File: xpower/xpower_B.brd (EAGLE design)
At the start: 80 x 80 mm, 41 parts, among them U1 TLV70233, U2 TLV70225, U3 STM1061N29, U4 ADM1085, U5 LM3674-ADJ

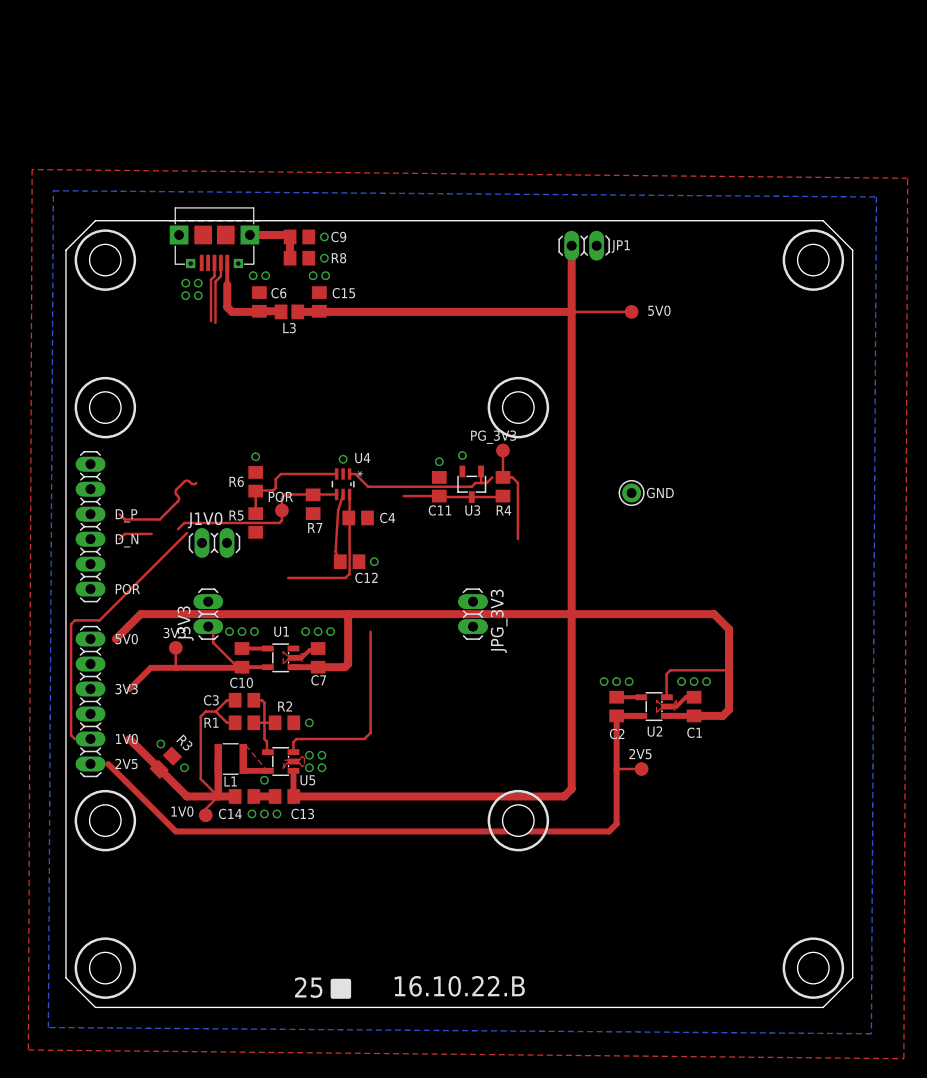
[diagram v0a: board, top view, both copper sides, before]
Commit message: xpower: B variant PCB finished
Signed-off-by: malo <pavol.malosek@gmail.com>
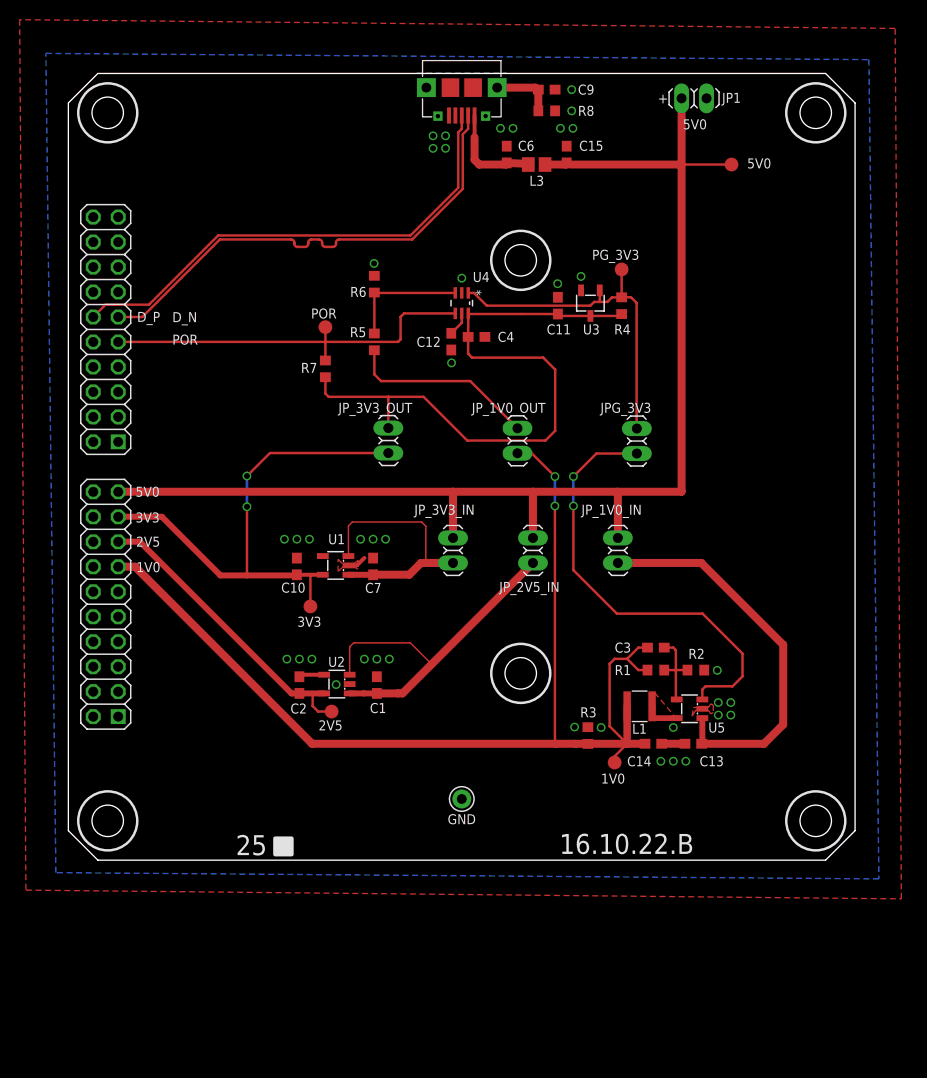
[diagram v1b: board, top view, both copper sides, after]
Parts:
- removed J1V0, J3V3: (no value), 25pinhead:1X02
- removed PWR1: (no value), 25cmsquare:LIWE_12_PIN_8X8_COMPAT
- added JP_1V0_IN, JP_2V5_IN, JP_3V3_IN: (no value), pinhead:1X02
- added JP_1V0_OUT, JP_3V3_OUT: (no value), 25pinhead:1X02
- added U$1: LIWE_40_PIN, 25cmsquare:LIWE_40_PIN_8X8
- C1, C7: value 1u, 0805 -> 1u, 0603; device rcl:C0805 -> rcl:C0603
- C10, C2: value 2u2, 0805 -> 2u2, 0603; device rcl:C0805 -> rcl:C0603
- C11, C15, C4, C6: value 100n, 0805 -> 100n, 0603; device rcl:C0805 -> rcl:C0603
- C12: value 2n2, 0805 -> 2n2, 0603; device rcl:C0805 -> rcl:C0603
- C13: value 4.7u, 0805 -> 4.7u, 0603; device rcl:C0805 -> rcl:C0603
- C14: value 10u, 0805 -> 10u, 0603; device rcl:C0805 -> rcl:C0603
- C3: value 18p, 0805 -> 18p, 0603; device rcl:C0805 -> rcl:C0603
- C9: value 4.7n, 0805 -> 4.7n, 0603; device rcl:C0805 -> rcl:C0603
- R1, R2: value 200k, 0805 -> 200k, 0603; device rcl:R0805 -> rcl:R0603
- R3: value 330, 0805 -> 330, 0603; device rcl:R0805 -> rcl:R0603
- R4, R6, R7: value 10k, 0805 -> 10k, 0603; device rcl:R0805 -> rcl:R0603
- R5: value 3k9, 0805 -> 3k9, 0603; device rcl:R0805 -> rcl:R0603
- R8: value 1M, 0805 -> 1M, 0603; device rcl:R0805 -> rcl:R0603
- moved R3 43.0 mm to (52.8, 12.7), turned to 270 degrees
- moved C3 42.2 mm to (59.7, 21.6)
- moved R1 42.2 mm to (59.7, 19.3)
- moved R2 42.2 mm to (63.8, 19.3)
- moved C13 41.9 mm to (63.6, 11.8)
- moved C14 41.9 mm to (59.5, 11.8)
- moved U5 41.9 mm to (63.2, 15.4)
- moved 1V0 41.9 mm to (55.5, 9.93)
- moved L1 41.9 mm to (59.7, 17.2)
- moved GND 35.6 mm to (40.0, 6.22)
- moved U2 32.3 mm to (27.3, 17.9)
- moved C1 32.3 mm to (31.4, 17.8)
- moved C2 32.3 mm to (23.5, 17.8)
- moved 2V5 32.1 mm to (26.8, 15.1)
- moved C15 29.3 mm to (50.7, 71.8)
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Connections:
- new net N$1: C1.1, JP_2V5_IN.1, U2.1, U2.3
- new net N$2: C7.1, JP_3V3_IN.1, U1.1, U1.3
- new net N$3: C13.1, JP_1V0_IN.1, U5.1
- net +1V0: now also JP_1V0_OUT.1, U$1.13; no longer J1V0.1, PWR1.2
- net +2V5: now also U$1.15; no longer PWR1.1
- net +3V3: now also JP_3V3_OUT.1, U$1.17; no longer J3V3.1, PWR1.4
- net +5V: now also JP_1V0_IN.2, JP_2V5_IN.2, JP_3V3_IN.2, U$1.19; no longer C1.1, C13.1, C7.1, PWR1.6, U1.1, U1.3, U2.1, U2.3, U5.1
- net D_N: now also U$1.111; no longer PWR1.9
- net D_P: now also U$1.112; no longer PWR1.10
- net GND: now also U$1.14, U$1.16, U$1.18, U$1.20; no longer PWR1.3, PWR1.8
- net J1V0: now also JP_1V0_OUT.2; no longer J1V0.2
- net J3V3: now also JP_3V3_OUT.2; no longer J3V3.2
- net POR: now also U$1.109; no longer PWR1.7
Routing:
- net +5V: track 219.1 -> 130.6 mm
- net +1V0: track 62.6 -> 116.6 mm, vias 0 -> 2
- net J3V3: track 24.7 -> 66.3 mm
- net N$3: track 0.00 -> 40.1 mm
- net D_N: track 9.81 -> 49.7 mm
- net +2V5: track 70.9 -> 31.9 mm
- net +3V3: track 22.1 -> 59.8 mm, vias 0 -> 2
- net N$1: track 0.00 -> 36.9 mm
- net D_P: track 16.6 -> 50.1 mm
- net N$2: track 0.00 -> 26.3 mm
- net PG_3V3: track 19.5 -> 45.6 mm, vias 0 -> 2
- net POR: track 18.9 -> 40.2 mm
- net J1V0: track 0.00 -> 19.3 mm
- net JPG_3V3: track 26.7 -> 34.9 mm
- net GND: track 13.4 -> 6.68 mm, vias 38 -> 39
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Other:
- board text added: "+"
- board text removed: "25cm"
- board text removed: "square.io"

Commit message: xpower: final tweaks
Signed-off-by: malo <pavol.malosek@gmail.com>
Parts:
- renumbered 1V0 to +1V0, 2V5 to +2V5, 3V3 to +3V3, 5V0 to +5V0
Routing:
- net GND: vias 39 -> 40
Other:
- board text added: "+1V0"
- board text added: "+2V5"
- board text added: "+3V3"
- board text added: "+5V0"
- board text removed: "1V0"
- board text removed: "2V5"
- board text removed: "3V3"
- board text removed: "5V0"
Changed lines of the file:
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@@
 <setting verticaltext="up"/>
 </settings>
-<grid distance="1" unitdist="mil" unit="mil" style="lines" multiple="1" display="yes" altdistance="0.025" altunitdist="inch" altunit="inch"/>
+<grid distance="3" unitdist="mil" unit="mil" style="lines" multiple="1" display="yes" altdistance="0.025" altunitdist="inch" altunit="inch"/>
 <layers>
 <layer number="1" name="Top" color="4" fill="1" visible="yes" active="yes"/>
@@
 <vertex x="56.5658" y="12.4714"/>
 </polygon>
-<text x="6.9088" y="29.7942" size="1.016" layer="25" font="vector" ratio="15" align="center-left">1V0</text>
-<text x="6.8834" y="32.385" size="1.016" layer="25" font="vector" ratio="15" align="center-left">2V5</text>
-<text x="6.8326" y="34.8488" size="1.016" layer="25" font="vector" ratio="15" align="center-left">3V3</text>
-<text x="6.8326" y="37.465" size="1.016" layer="25" font="vector" ratio="15" align="center-left">5V0</text>
+<text x="6.9088" y="29.7942" size="1.016" layer="25" font="vector" ratio="15" align="center-left">+1V0</text>
+<text x="6.8834" y="32.385" size="1.016" layer="25" font="vector" ratio="15" align="center-left">+2V5</text>
+<text x="6.8326" y="34.8488" size="1.016" layer="25" font="vector" ratio="15" align="center-left">+3V3</text>
+<text x="6.8326" y="37.465" size="1.016" layer="25" font="vector" ratio="15" align="center-left">+5V0</text>
 <text x="10.5664" y="52.9336" size="1.016" layer="25" font="vector" ratio="15" align="center-left">POR</text>
 <text x="10.5664" y="55.2196" size="1.016" layer="25" font="vector" ratio="15" align="center-left">D_N</text>
@@
 <vertex x="22.7076" y="0.5842"/>
 </polygon>
-<text x="62.484" y="74.8284" size="1.016" layer="25" font="vector" ratio="15" align="center-left">5V0</text>
+<text x="61.849" y="74.803" size="1.016" layer="25" font="vector" ratio="15" align="center-left">+5V0</text>
 <text x="59.944" y="77.47" size="1.016" layer="25" font="vector" ratio="15" align="center-left">+</text>
 </plain>
@@
 <attribute name="NAME" x="51.943" y="72.136" size="1.016" layer="25" font="vector" ratio="15"/>
 </element>
-<element name="1V0" library="testpad" package="TP14R" value="TPTP14R" x="55.5498" y="9.9314" smashed="yes">
+<element name="+1V0" library="testpad" package="TP14R" value="TPTP14R" x="55.5498" y="9.9314" smashed="yes">
 <attribute name="TP_SIGNAL_NAME" value="" x="55.5498" y="7.3914" size="1" layer="37"/>
-<attribute name="NAME" x="54.164" y="7.7859" size="1.016" layer="25" font="vector" ratio="15"/>
-</element>
-<element name="2V5" library="testpad" package="TP14R" value="TPTP14R" x="26.7716" y="15.113" smashed="yes">
+<attribute name="NAME" x="53.5798" y="7.7859" size="1.016" layer="25" font="vector" ratio="15"/>
+</element>
+<element name="+2V5" library="testpad" package="TP14R" value="TPTP14R" x="26.7716" y="15.113" smashed="yes">
 <attribute name="TP_SIGNAL_NAME" value="" x="26.7716" y="12.573" size="1" layer="37"/>
-<attribute name="NAME" x="25.4366" y="13.1961" size="1.016" layer="25" font="vector" ratio="15"/>
-</element>
-<element name="3V3" library="testpad" package="TP14R" value="TPTP14R" x="24.6126" y="25.8064" smashed="yes">
+<attribute name="NAME" x="24.7254" y="13.0945" size="1.016" layer="25" font="vector" ratio="15"/>
+</element>
+<element name="+3V3" library="testpad" package="TP14R" value="TPTP14R" x="24.6126" y="25.8064" smashed="yes">
 <attribute name="TP_SIGNAL_NAME" value="" x="24.6126" y="23.2664" size="1" layer="37"/>
-<attribute name="NAME" x="23.2776" y="23.7371" size="1.016" layer="25" font="vector" ratio="15"/>
-</element>
-<element name="5V0" library="testpad" package="TP14R" value="TPTP14R" x="67.437" y="70.739" smashed="yes">
+<attribute name="NAME" x="22.795" y="23.7371" size="1.016" layer="25" font="vector" ratio="15"/>
+</element>
+<element name="+5V0" library="testpad" package="TP14R" value="TPTP14R" x="67.437" y="70.739" smashed="yes">
 <attribute name="TP_SIGNAL_NAME" value="" x="67.437" y="68.199" size="1" layer="37"/>
 <attribute name="NAME" x="69.023" y="70.3461" size="1.016" layer="25" font="vector" ratio="15"/>
@@
 <wire x1="48.475" y1="70.739" x2="50.607" y2="70.739" width="0.8128" layer="1"/>
 <wire x1="50.607" y1="70.739" x2="50.673" y2="70.905" width="0.8128" layer="1"/>
-<contactref element="5V0" pad="TP"/>
+<contactref element="+5V0" pad="TP"/>
 <wire x1="50.673" y1="70.905" x2="51.181" y2="70.805" width="0.254" layer="1"/>
 <wire x1="51.181" y1="70.805" x2="51.181" y2="70.739" width="0.254" layer="1"/>
@@
 <via x="38.354" y="73.66" extent="1-16" drill="0.6" shape="square"/>
 <via x="37.084" y="73.66" extent="1-16" drill="0.6" shape="square"/>
-<via x="45.212" y="74.422" extent="1-16" drill="0.6" shape="square"/>
-<via x="43.942" y="74.422" extent="1-16" drill="0.6" shape="square"/>
-<via x="51.308" y="74.422" extent="1-16" drill="0.6" shape="square"/>
-<via x="50.038" y="74.422" extent="1-16" drill="0.6" shape="square"/>
-<via x="21.971" y="32.639" extent="1-16" drill="0.6" shape="square"/>
-<via x="23.241" y="32.639" extent="1-16" drill="0.6" shape="square"/>
-<via x="24.511" y="32.639" extent="1-16" drill="0.6" shape="square"/>
+<via x="45.212" y="73.9902" extent="1-16" drill="0.6" shape="square"/>
+<via x="43.9674" y="73.9902" extent="1-16" drill="0.6" shape="square"/>
+<via x="51.2318" y="74.0156" extent="1-16" drill="0.6" shape="square"/>
+<via x="50.1142" y="74.0156" extent="1-16" drill="0.6" shape="square"/>
+<via x="23.0124" y="32.4104" extent="1-16" drill="0.6" shape="square"/>
+<via x="24.384" y="32.4104" extent="1-16" drill="0.6" shape="square"/>
+<via x="25.7556" y="32.4104" extent="1-16" drill="0.6" shape="square"/>
 <via x="38.9636" y="50.5714" extent="1-16" drill="0.6" shape="square"/>
 <via x="40.005" y="59.182" extent="1-16" drill="0.6" shape="square"/>
@@
 <via x="30.988" y="32.639" extent="1-16" drill="0.6" shape="square"/>
 <via x="32.258" y="32.639" extent="1-16" drill="0.6" shape="square"/>
-<via x="22.225" y="20.447" extent="1-16" drill="0.6" shape="square"/>
-<via x="23.495" y="20.447" extent="1-16" drill="0.6" shape="square"/>
-<via x="24.765" y="20.447" extent="1-16" drill="0.6" shape="square"/>
+<via x="23.2156" y="20.1422" extent="1-16" drill="0.6" shape="square"/>
+<via x="24.4602" y="20.1422" extent="1-16" drill="0.6" shape="square"/>
+<via x="25.7556" y="20.1422" extent="1-16" drill="0.6" shape="square"/>
 <via x="60.2488" y="10.0584" extent="1-16" drill="0.6" shape="square"/>
 <via x="61.5188" y="10.0584" extent="1-16" drill="0.6" shape="square"/>
@@
 <via x="51.4858" y="13.5382" extent="1-16" drill="0.6" shape="square"/>
 <via x="54.1782" y="13.4874" extent="1-16" drill="0.6" shape="square"/>
-<polygon width="0.254" layer="1" thermals="no">
-<vertex x="63.5508" y="15.5194"/>
-<vertex x="65.0748" y="15.5194"/>
-<vertex x="65.3288" y="15.9004"/>
-<vertex x="65.5828" y="15.7734"/>
-<vertex x="65.5828" y="15.0114"/>
-<vertex x="65.3288" y="14.8844"/>
-<vertex x="65.0748" y="15.2654"/>
-<vertex x="63.8048" y="15.2654"/>
-<vertex x="63.4238" y="14.6304"/>
-</polygon>
 <via x="61.5188" y="13.4874" extent="1-16" drill="0.6" shape="square"/>
 <polygon width="0.254" layer="1" thermals="no">
@@
 <contactref element="U$1" pad="14"/>
 <via x="27.2288" y="17.8562" extent="1-16" drill="0.6" shape="square"/>
+<via x="27.178" y="29.972" extent="1-16" drill="0.6" shape="square"/>
 </signal>
 <signal name="+3V3">
@@
 <wire x1="23.053" y1="28.956" x2="18.161" y2="28.956" width="0.6096" layer="1"/>
 <wire x1="18.161" y1="28.956" x2="15.4686" y2="28.956" width="0.6096" layer="1"/>
-<contactref element="3V3" pad="TP"/>
+<contactref element="+3V3" pad="TP"/>
 <contactref element="JP_3V3_OUT" pad="1"/>
 <contactref element="U$1" pad="17"/>
@@
 <contactref element="C2" pad="1"/>
 <wire x1="26.005" y1="16.957" x2="23.495" y2="16.9554" width="0.6096" layer="1"/>
-<contactref element="2V5" pad="TP"/>
+<contactref element="+2V5" pad="TP"/>
 <contactref element="U$1" pad="15"/>
 <wire x1="23.495" y1="16.9554" x2="22.694" y2="16.9554" width="0.6096" layer="1"/>
@@
 <wire x1="56.8198" y1="20.4724" x2="57.9628" y2="19.3294" width="0.254" layer="1"/>
 <wire x1="57.9628" y1="19.3294" x2="58.8908" y2="19.3294" width="0.254" layer="1"/>
-<contactref element="1V0" pad="TP"/>
+<contactref element="+1V0" pad="TP"/>
 <wire x1="56.8198" y1="11.8364" x2="55.5498" y2="10.5664" width="0.254" layer="1"/>
 <wire x1="55.5498" y1="10.5664" x2="55.5498" y2="9.9314" width="0.254" layer="1"/>
@@
 <contactref element="JP_3V3_OUT" pad="2"/>
 <wire x1="40.6654" y1="55.6006" x2="40.6908" y2="55.626" width="0.254" layer="1"/>
-<wire x1="46.1112" y1="55.5396" x2="49.784" y2="55.538" width="0.254" layer="1"/>
 <wire x1="49.784" y1="55.538" x2="49.88" y2="55.342" width="0.254" layer="1"/>
 <wire x1="49.88" y1="55.342" x2="53.086" y2="55.342" width="0.254" layer="1"/>
 <wire x1="56.261" y1="55.538" x2="56.165" y2="55.342" width="0.254" layer="1"/>
 <wire x1="56.165" y1="55.342" x2="53.086" y2="55.342" width="0.254" layer="1"/>
-<wire x1="46.1112" y1="55.5396" x2="40.7264" y2="55.5396" width="0.254" layer="1"/>
 <wire x1="40.7264" y1="55.5396" x2="40.6654" y2="55.6006" width="0.254" layer="1"/>
 <wire x1="40.6536" y1="53.213" x2="40.6654" y2="53.2248" width="0.254" layer="1"/>
@@
 <wire x1="41.0464" y1="51.1048" x2="40.6536" y2="51.4976" width="0.254" layer="1"/>
 <wire x1="40.6536" y1="51.4976" x2="40.6536" y2="53.213" width="0.254" layer="1"/>
+<wire x1="40.7264" y1="55.5396" x2="49.784" y2="55.5396" width="0.254" layer="1"/>
+<wire x1="49.784" y1="55.5396" x2="49.784" y2="55.538" width="0.254" layer="1"/>
 </signal>
 <signal name="JPG_3V3">
